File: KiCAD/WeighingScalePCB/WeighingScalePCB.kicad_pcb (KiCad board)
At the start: 2 copper layers, 94.6 x 73.3 mm, 64 parts, among them IC1 MAX6675ISA+T, IC2 APS11753KMDALX-9PL5, J1 Conn_01x14_MountingPin, J2 AudioJack4, J4 Battery Conn, J6 Conn_01x04_MountingPin, Q2 NX138AKR, Q3 NX138AKR, Q4 NX138AKR, Q5 NX138AKR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

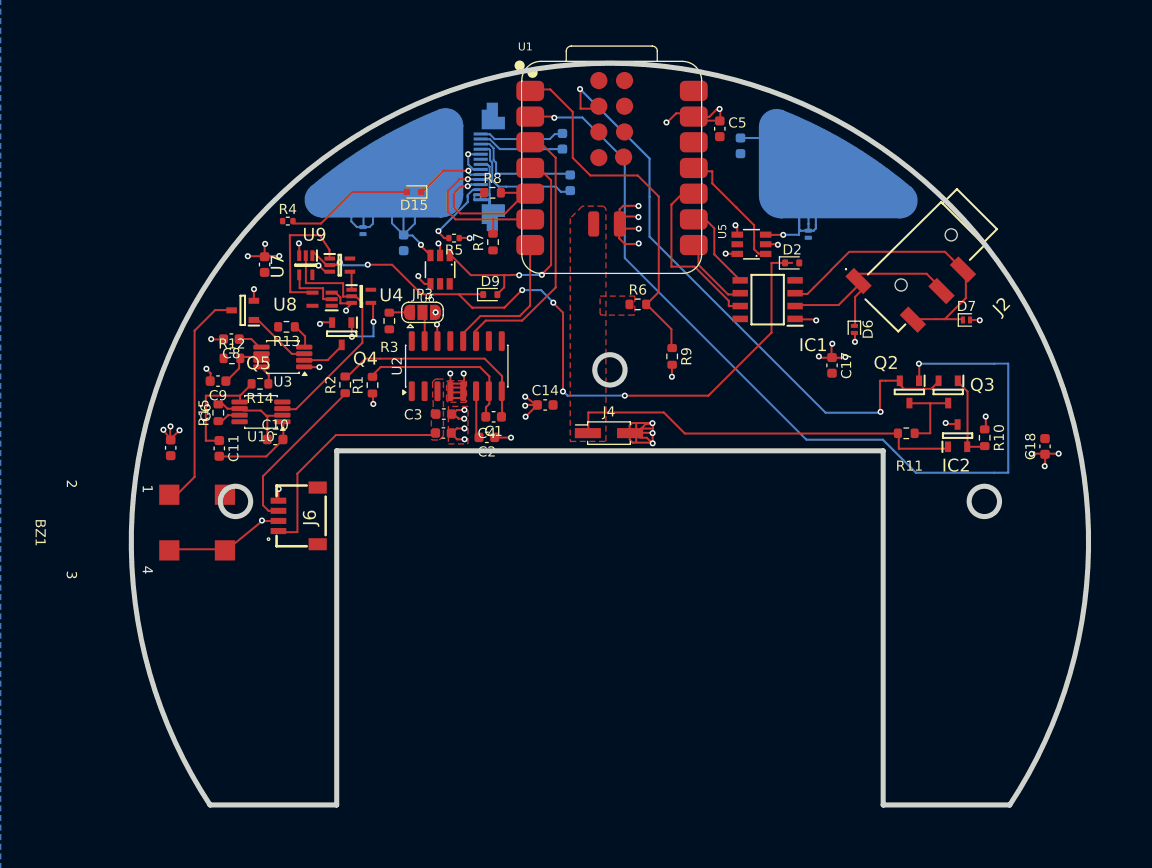
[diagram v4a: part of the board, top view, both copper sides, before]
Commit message: buzzer and J2 3d pending, design doc pending, edge cuts modified to remove redundant area, mounting holes are now m2 compatible
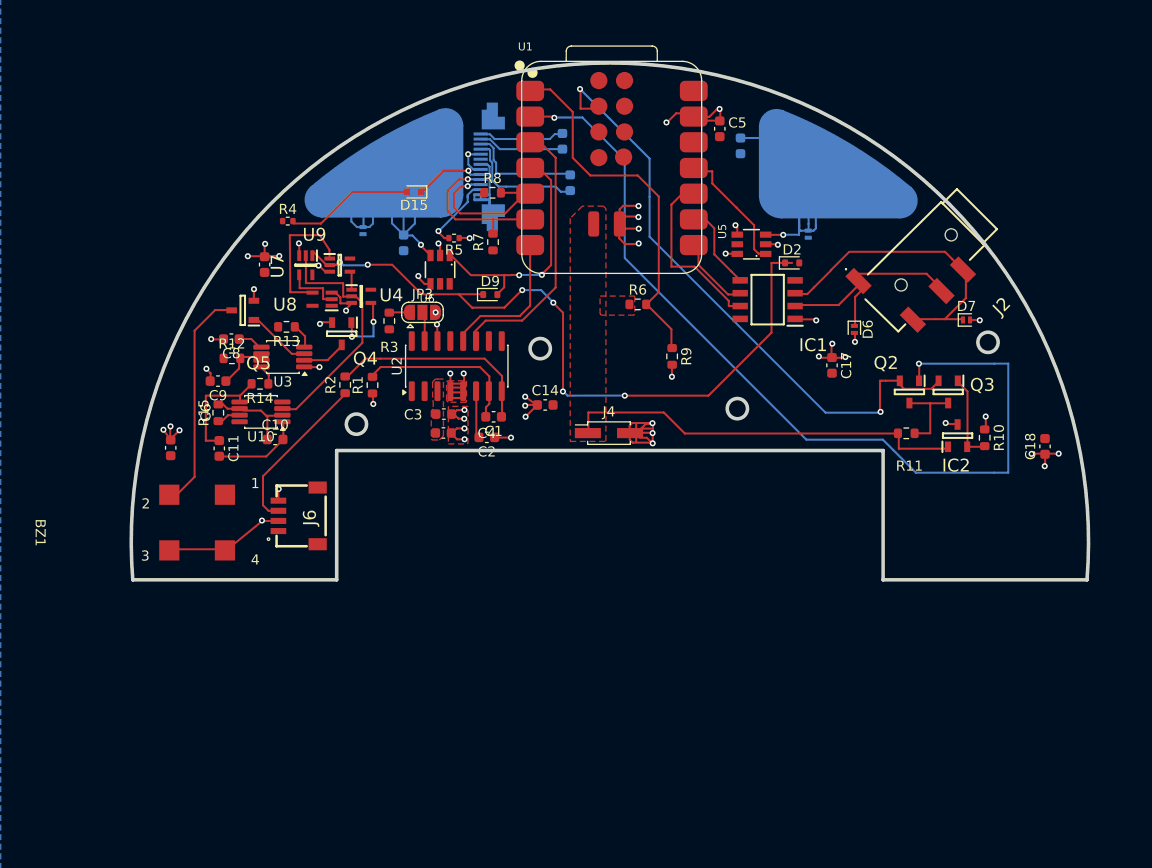
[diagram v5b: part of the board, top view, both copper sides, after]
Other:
- board size 94.6 x 73.3 mm -> 94.6 x 51.1 mm
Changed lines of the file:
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@@
 		)
 		(fp_text user "3"
-			(at 4.25 3.75 270)
+			(at 3.38 -3.69 0)
 			(unlocked yes)
 			(layer "F.SilkS")
@@
 		)
 		(fp_text user "2"
-			(at -4.75 3.75 270)
+			(at -1.77 -3.75 0)
 			(unlocked yes)
 			(layer "F.SilkS")
@@
 		)
 		(fp_text user "4"
-			(at 3.75 -3.75 270)
+			(at 3.77 -14.56 0)
 			(unlocked yes)
 			(layer "F.SilkS")
@@
 		)
 		(fp_text user "1"
-			(at -4.25 -3.75 270)
+			(at -3.78 -14.56 0)
 			(unlocked yes)
 			(layer "F.SilkS")
@@
 	)
 	(gr_line
-		(start 119.81 73.51)
-		(end 129.33 73.51)
-		(stroke
-			(width 0.2)
-			(type default)
-		)
-		(layer "F.Cu")
-		(net 8)
-	)
-	(gr_line
 		(start 148.37 54.64)
 		(end 149.79 54.64)
@@
 	)
 	(gr_line
-		(start 114.06 83.11)
-		(end 116 83.11)
-		(stroke
-			(width 0.2)
-			(type default)
-		)
-		(layer "F.Cu")
-		(net 8)
-	)
-	(gr_line
 		(start 103.43 73.935)
 		(end 104.35 73.04)
@@
 	)
 	(gr_line
-		(start 116 83.11)
-		(end 116 77.32)
-		(stroke
-			(width 0.2)
-			(type default)
-		)
-		(layer "F.Cu")
-		(net 8)
-	)
-	(gr_line
 		(start 183.96 74.67)
 		(end 182.27 74.67)
@@
 	)
 	(gr_line
-		(start 116 77.32)
-		(end 119.81 73.51)
-		(stroke
-			(width 0.2)
-			(type default)
-		)
-		(layer "F.Cu")
-		(net 8)
-	)
-	(gr_line
 		(start 123.48 60.52)
 		(end 123.48 62.27)
@@
 	)
 	(gr_line
-		(start 119.883161 110.07)
-		(end 119.883161 75.07)
+		(start 119.88 75.041353)
+		(end 119.88 87.818647)
 		(stroke
-			(width 0.5)
+			(width 0.35)
 			(type default)
 		)
 		(layer "Edge.Cuts")
 	)
-	(gr_circle
-		(center 146.883162 67.07)
-		(end 148.383162 67.07)
+	(gr_line
+		(start 173.880001 87.818647)
+		(end 194.028935 87.818647)
 		(stroke
-			(width 0.5)
+			(width 0.35)
 			(type default)
 		)
-		(fill no)
 		(layer "Edge.Cuts")
 	)
-	(gr_arc
-		(start 107.37 110.07)
-		(mid 146.883162 36.77)
-		(end 186.396324 110.07)
+	(gr_line
+		(start 173.880001 75.041353)
+		(end 119.88 75.041353)
 		(stroke
-			(width 0.5)
+			(width 0.35)
 			(type default)
 		)
 		(layer "Edge.Cuts")
 	)
-	(gr_circle
-		(center 109.883161 80.07)
-		(end 111.383161 80.07)
+	(gr_arc
+		(start 99.731067 87.818647)
+		(mid 146.880001 36.741352)
+		(end 194.028935 87.818647)
 		(stroke
-			(width 0.5)
+			(width 0.35)
 			(type default)
 		)
-		(fill no)
 		(layer "Edge.Cuts")
 	)
 	(gr_circle
-		(center 183.883162 80.07)
-		(end 185.383162 80.07)
+		(center 159.477039 70.901954)
+		(end 160.477039 70.901954)
 		(stroke
-			(width 0.5)
+			(width 0.35)
 			(type default)
 		)
@@
 	)
 	(gr_line
-		(start 173.883162 110.07)
-		(end 186.396324 110.07)
+		(start 173.880001 87.818647)
+		(end 173.880001 75.041353)
 		(stroke
-			(width 0.5)
+			(width 0.35)
 			(type default)
 		)
@@
 	)
 	(gr_line
-		(start 119.883161 75.07)
-		(end 173.883162 75.07)
+		(start 99.731067 87.818647)
+		(end 119.88 87.818647)
 		(stroke
-			(width 0.5)
+			(width 0.35)
 			(type default)
 		)
 		(layer "Edge.Cuts")
 	)
-	(gr_line
-		(start 173.883162 75.07)
-		(end 173.883162 110.07)
+	(gr_circle
+		(center 121.834017 72.435558)
+		(end 122.834017 72.435558)
 		(stroke
-			(width 0.5)
+			(width 0.35)
 			(type default)
 		)
+		(fill no)
 		(layer "Edge.Cuts")
 	)
-	(gr_line
-		(start 107.37 110.07)
-		(end 119.883161 110.07)
+	(gr_circle
+		(center 139.996841 64.971354)
+		(end 140.996841 64.971354)
 		(stroke
-			(width 0.5)
+			(width 0.35)
 			(type default)
 		)
+		(fill no)
+		(layer "Edge.Cuts")
+	)
+	(gr_circle
+		(center 184.247077 64.34928)
+		(end 185.247077 64.34928)
+		(stroke
+			(width 0.35)
+			(type default)
+		)
+		(fill no)
 		(layer "Edge.Cuts")
 	)
@@
 	)
 	(group ""
-		(members "1e24307c-1187-4a6f-b6bf-d1ce7814f20a" "3e15cb58-223b-4983-b375-76b0a59fe2e5"
-			"4bb72ed9-cd55-44f9-879c-921b48c02bec" "621680a9-33c3-4bb3-a35e-eef1ae0175da"
-			"86e81114-9e1e-427d-a412-39e565bd073f" "9eec9fcb-2d9f-4e18-82b9-857fe2e4cfae"
-			"ad9043c9-0c5a-40de-b816-01694950fc25" "c910cb29-fa94-4e6e-bf7d-f2e11731123c"
-			"e3c6ae85-94df-4515-a09d-367b8bbcd14e"
+		(members "33877af2-a4c7-45f0-b117-d1c529e0dbed" "541224a9-8fb9-4458-8c51-e2adba2ced66"
+			"5fb170d9-5793-40b4-b85f-c5e7b7321e78" "8d9a365d-87be-45fe-b917-807a15a55aa8"
+			"8e723126-0adf-418b-8854-cde6beea1bcf" "8edc17c6-b37a-4c3f-8315-1ed8aa0b869f"
+			"9eedef8a-3057-410b-9d83-6461c7000d45" "af9d2442-1edc-4e79-8749-d5750aad559e"
+			"dd133048-9653-4f8d-aa13-adb510ca6ec6" "e85c6d3f-0aff-4fe7-80a3-903b76ab98d0"
 		)
 	)

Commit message: changed touch sensor to CAP1203, yet to update in layout schematic done.
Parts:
- removed C10, C11, C8: 0.1u, Capacitor_SMD:C_0603_1608Metric
- removed C15, C16: 22pF, Capacitor_SMD:C_0603_1608Metric
- removed C9: 1u, Capacitor_SMD:C_0603_1608Metric
- removed D2, D9: 1N4148WT, Diode_SMD:D_SOD-523
- removed D3, D4: PESD3V3U1UL, Diode_SMD:D_SOD-882
- removed Q4: NX138AKR, Footprints:SOT95P230X110-3N
- removed R12: 470K, Resistor_SMD:R_0603_1608Metric
- removed R13: 10K, Resistor_SMD:R_0603_1608Metric
- removed R14, R15: R_US, Resistor_SMD:R_0603_1608Metric
- removed U10: LMC555xMM, Package_SO:VSSOP-8_3x3mm_P0.65mm
- removed U4, U7: 74LVC1G79GW-Q100H, Footprints:SOT65P212X110-5N_D_FF
- removed U5, U6: TTP223-BA6, Footprints:SOT23-6_touchpad_sensor
- removed U8: 74LVC1G04, Footprints:SOT65P210X110-5N_NOT
- removed U9: 74LVC1G08, Footprints:SOT65P212X110-5N_AND
- U3: value LMC555xMM -> LMC555xM; footprint Package_SO:VSSOP-8_3x3mm_P0.65mm -> Package_SO:SOIC-8_3.9x4.9mm_P1.27mm
- moved U3 36.8 mm to (146.5, 84.0), turned to 0 degrees
- turned C13 to 90 degrees
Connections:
- net /buzz_drive renamed Net-(Q5-G)
- T1 pad T1: /touch1 -> Net-(IC3-CS1)
- T2 pad T2: /touch2 -> Net-(IC3-CS2)
- U1 pad 11: Tare -> unconnected-(U1-GPIO18_D10_MOSI-Pad11)
- U1 pad 4: Time -> /touch
- U3 pad 2: /buzz_pull_down -> /touch
- U3 pad 4: Net-(U3-R) -> VCC
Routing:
- net VCC: vias 1 -> 3
- net Time: vias 2 -> 0
- net Net-(IC3-CS2): vias 0 -> 1
- net Net-(IC3-CS1): vias 0 -> 1
- net /touch2: vias 1 -> 0
- net /touch1: vias 1 -> 0
- net /touch: vias 0 -> 2
- net /timeORtare: vias 6 -> 0
- net /buzzer trigger: vias 2 -> 0
- net (no net): vias 0 -> 8
- removed copper zone on F.Cu, net GND
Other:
- board text removed: "${REFERENCE}"

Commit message: DRCs cleared
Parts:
- removed Q2, Q3: NX138AKR, Footprints:SOT95P230X110-3N
- removed R10: 1K, Resistor_SMD:R_0603_1608Metric
- removed R11: 5K, Resistor_SMD:R_0603_1608Metric
- added C10: 0.1u, Capacitor_SMD:C_0603_1608Metric, F.Cu at (145.5, 69.7)
- added C11: 0.1u, Capacitor_SMD:C_0603_1608Metric, F.Cu at (131.5, 73.6)
- added C15: 10u, Capacitor_SMD:C_0603_1608Metric, F.Cu at (137.2, 65.5)
- added C8: 0.01u, Capacitor_SMD:C_0603_1608Metric, F.Cu at (139.6, 72.1)
- added C9: 1u, Capacitor_SMD:C_0603_1608Metric, F.Cu at (145.5, 71.7)
- added IC3: CAP1203-1-SN, Footprints:CAP1203_SOIC127P600X175-8N, F.Cu at (145.6, 65.6)
- added R12: 47k, Resistor_SMD:R_0603_1608Metric, F.Cu at (139.3, 69.2)
- added R13: 220k, Resistor_SMD:R_0603_1608Metric, F.Cu at (113.5, 86.2)
- added U4: 74LVC1G32, Footprints:SOT95P285X140-5N, F.Cu at (134.1, 63.5)
- R4: value 10K -> 10k
- R7, R8: value 10K -> 4.7k
- moved IC2 44.0 mm to (139.1, 60.9), turned to -90 degrees
- moved C18 29.0 mm to (168.0, 55.5), turned to 180 degrees
- moved C14 27.6 mm to (113.0, 71.9), turned to 90 degrees
- moved U3 19.0 mm to (133.7, 69.9)
- moved Q5 15.0 mm to (104.7, 75.0)
- moved J4 12.1 mm to (146.9, 61.2)
- moved C2 11.3 mm to (125.0, 68.0), turned to 90 degrees
- moved JP3 9.12 mm to (120.2, 57.3)
- moved U2 9.12 mm to (123.6, 62.6)
- moved C4 9.12 mm to (122.3, 69.2)
- moved R3 9.12 mm to (116.9, 58.1)
- moved C3 9.12 mm to (122.3, 67.3)
- moved C1 9.11 mm to (127.3, 67.6)
- moved C6 7.73 mm to (106.7, 67.7)
- moved R2 7.49 mm to (128.1, 69.8)
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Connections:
- net Net-(J6-Pin_3) renamed /load_P
- BZ1 pad 1: VCC -> Net-(BZ1-+-Pad1)
- J6 pad 4: GND -> /load_N
- R1 pad 1: GND -> /load_N
- U1 pad 11: unconnected-(U1-GPIO18_D10_MOSI-Pad11) -> /touch
- U1 pad 19: /enable -> unconnected-(U1-CHIP_EN-Pad19)
- U1 pad 4: /touch -> /enable
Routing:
- net GND: track 0.00 -> 69.4 mm, vias 56 -> 47
- net /touch: track 0.00 -> 57.5 mm, vias 2 -> 0
- net /ble_keep_awake: track 0.00 -> 41.9 mm, vias 2 -> 0
- net Net-(Q5-G): track 0.00 -> 41.4 mm
- net Net-(IC3-CS1): track 0.00 -> 33.5 mm, vias 1 -> 3
- net PD_SCK: track 0.00 -> 31.2 mm
- net Net-(IC3-CS2): track 0.00 -> 30.8 mm
- net /enable: track 0.00 -> 30.0 mm
- net /T-: track 0.00 -> 29.6 mm
- net SCL: track 0.00 -> 28.4 mm, vias 1 -> 3
- net SDA: track 0.00 -> 22.0 mm, vias 1 -> 3
- net /load_P: track 0.00 -> 21.5 mm
- net /load_N: track 0.00 -> 18.9 mm
- net DOut: track 0.00 -> 17.6 mm
- net /T+: track 0.00 -> 17.5 mm
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- removed copper zone on F.Cu, net /V_BAT
